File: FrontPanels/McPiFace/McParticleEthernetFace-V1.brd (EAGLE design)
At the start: 44 x 88 mm, 10 parts

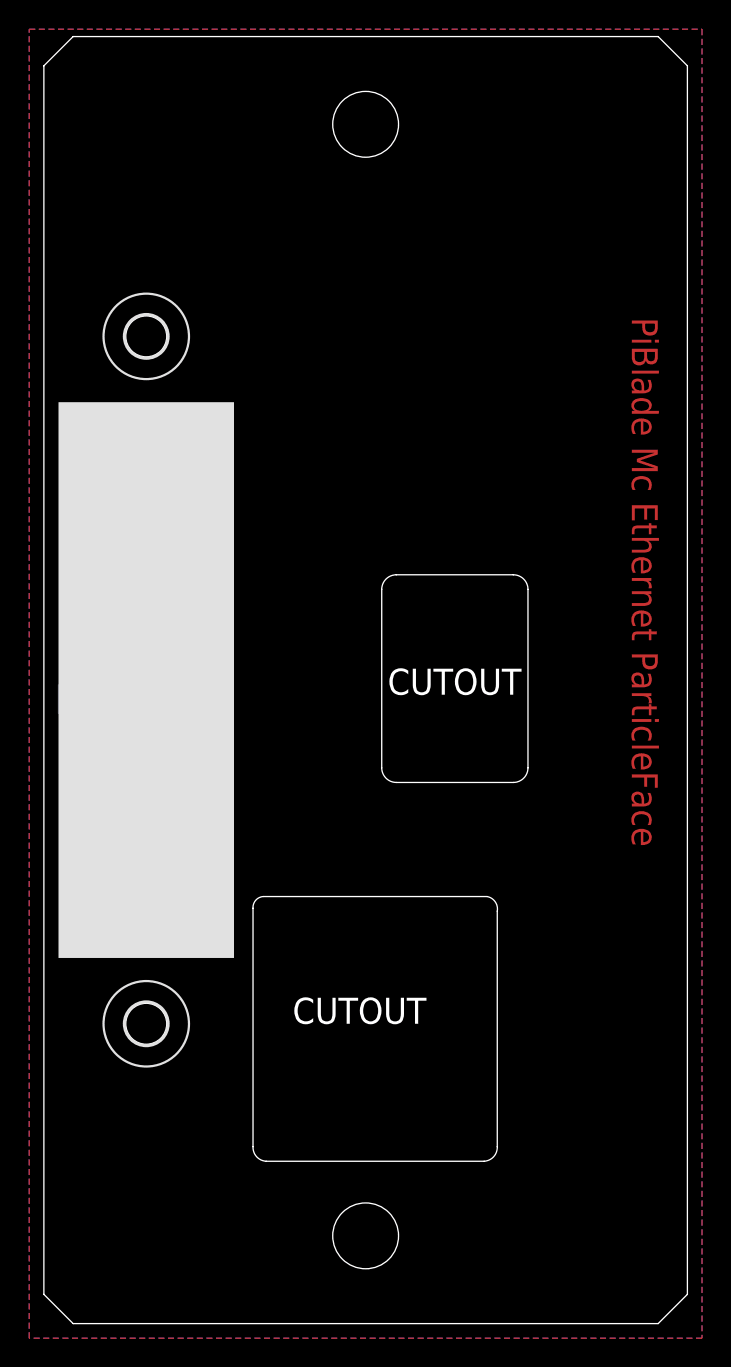
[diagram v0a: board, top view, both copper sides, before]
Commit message: Fixed height of ethernet connector.
Moved LEDs/connector as the frame clashes with that area of the panel.
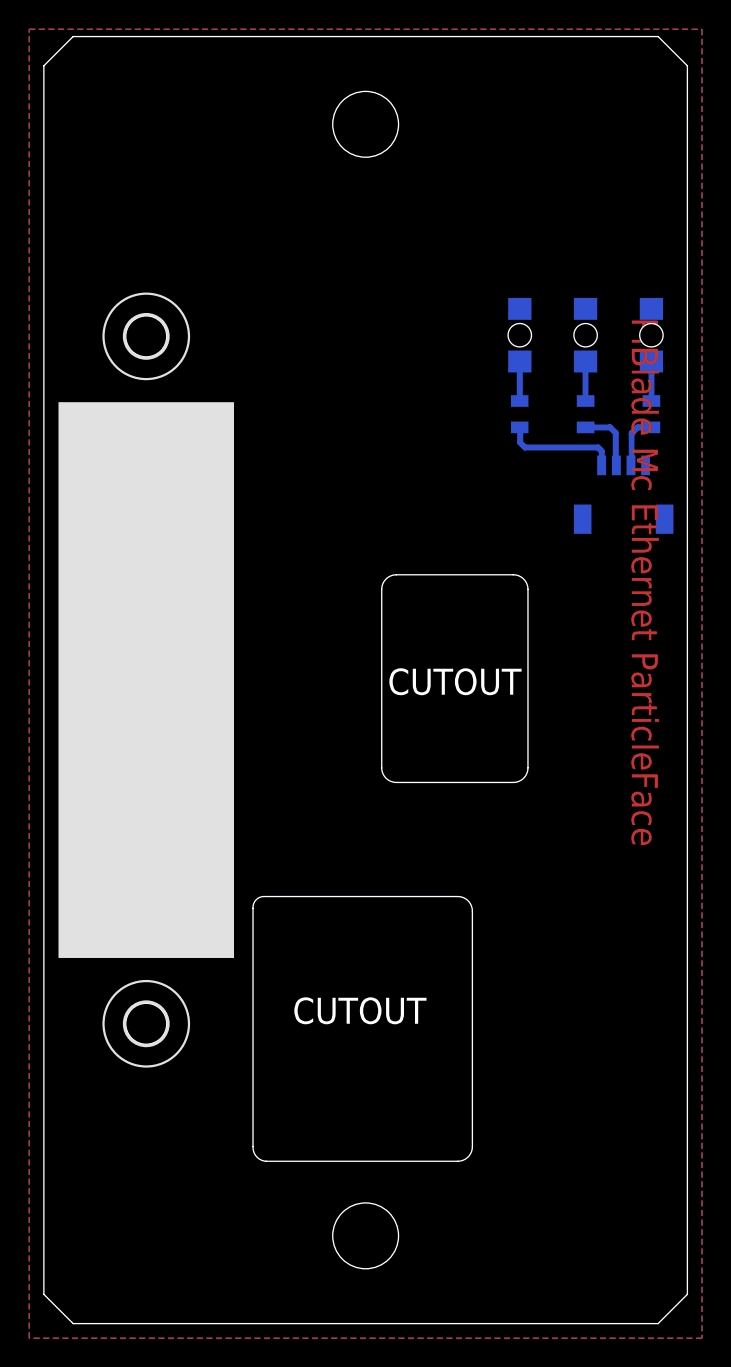
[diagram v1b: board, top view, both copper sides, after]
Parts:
- moved D3 53.9 mm to (41.5, 67.6), turned to 90 degrees
- moved D2 47.8 mm to (37.0, 67.6), turned to 90 degrees
- moved R1 47.3 mm to (41.5, 62.2), turned to 90 degrees
- moved D1 42.7 mm to (32.5, 67.6), turned to 90 degrees
- moved J1 40.4 mm to (39.6, 58.7), turned to 0 degrees
- moved R2 40.2 mm to (37.0, 62.2), turned to 90 degrees
- moved R3 34.0 mm to (32.5, 62.2), turned to 90 degrees
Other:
- outline, holes or cut-outs redrawn
